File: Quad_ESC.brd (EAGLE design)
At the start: 100 x 80 mm, 25 parts, among them U1 SN74CBTLV3257PWR, Y1 ECS-80-S-4X

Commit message: Lib Update (again)
ok definitely did not push the wrong version of the library file last time haha
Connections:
- net NRST_IN: no longer U$2.P$21
- net SWCLK_IN: no longer U$2.P$19
- net SWDIO_IN: no longer U$2.P$20
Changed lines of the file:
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@@
 <signal name="SWCLK_IN">
 <contactref element="U1" pad="P$4"/>
-<contactref element="U$2" pad="P$19"/>
-<wire x1="-77.47" y1="87.63" x2="-69.85" y2="-10.16" width="0" layer="19" extent="1-1"/>
 </signal>
 <signal name="SWDIO_IN">
 <contactref element="U1" pad="P$7"/>
-<contactref element="U$2" pad="P$20"/>
-<wire x1="-77.47" y1="83.82" x2="-67.31" y2="-10.16" width="0" layer="19" extent="1-1"/>
 </signal>
 <signal name="NRST_IN">
 <contactref element="U1" pad="P$9"/>
-<contactref element="U$2" pad="P$21"/>
-<wire x1="-72.07" y1="82.55" x2="-64.77" y2="-10.16" width="0" layer="19" extent="1-1"/>
 </signal>
 <signal name="N$3">

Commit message: Lib Update/Sch Update
Migrated 3 pin connectors from X-11 AFRO lib; fixed BLHeli symbol so labels no longer overlap; fixed connections and placement on schematic.
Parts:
- added SV2: (no value), con-lsta:FE05-1
- added U$5, U$6, U$7: 3PINCONNECTOR, BLHeli_32 45A:3PINCONNECTOR
- added U$9: BL_HELI45A, BLHeli_32 45A:BLHELI_20X20
- U$1: value BL_HELI45A -> 3PINCONNECTOR; device BLHeli_32 45A:BLHELI_20X20 -> BLHeli_32 45A:3PINCONNECTOR
- moved C10 272.6 mm to (-81.3, -138.4)
- moved U$8 251.8 mm to (-81.3, -134.6)
- moved U$1 15.5 mm to (-72.4, -54.6)
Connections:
- new net ESC1_B: U$1.A, U$9.P$1
- new net ESC1_R: U$1.C, U$9.P$3
- new net ESC1_Y: U$1.B, U$9.P$2
- new net ESC2_B: U$5.A, U$9.P$4
- new net ESC2_R: U$5.C, U$9.P$6
- new net ESC2_Y: U$5.B, U$9.P$5
- new net ESC3_B: U$6.A, U$9.P$7
- new net ESC3_R: U$6.C, U$9.P$9
- new net ESC3_Y: U$6.B, U$9.P$8
- new net ESC4_B: U$7.A, U$9.P$10
- new net ESC4_R: U$7.C, U$9.P$12
- new net ESC4_Y: U$7.B, U$9.P$11
- new net N$31: U$9.P$17
- new net N$32: U$9.P$18
- new net TIM3_CH1: U$4.PA6, U$9.P$19
- new net TIM3_CH2: U$4.PA7, U$9.P$20
- new net TIM3_CH3: U$4.PB0, U$9.P$21
- new net TIM3_CH4: U$4.PB1, U$9.P$22
- net +12V: now also U$9.P$14
- net +3V3: now also SV2.5
- net GND: now also SV2.3, U$9.P$13, U$9.P$15, U$9.P$16
- net NRST_IN: now also SV2.1
- net SWCLK_IN: now also SV2.4
- net SWDIO_IN: now also SV2.2

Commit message: Board Update
Added minor pin connections
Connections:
- removed net N$3: R4.1, U1.P$15
- new net PROG_SEL: R4.1, U$2.P$5, U1.P$15
- net CAN_H: now also U$2.P$6
- net CAN_L: now also U$2.P$7
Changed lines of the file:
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@@
 <wire x1="-72.07" y1="82.55" x2="-78.74" y2="-143.51" width="0" layer="19" extent="1-1"/>
 </signal>
-<signal name="N$3">
+<signal name="PROG_SEL">
 <contactref element="U1" pad="P$15"/>
 <contactref element="R4" pad="1"/>
+<contactref element="U$2" pad="P$5"/>
+<wire x1="-69.85" y1="-12.7" x2="-82.13" y2="-6.35" width="0" layer="19" extent="1-1"/>
 <wire x1="-72.07" y1="90.17" x2="-82.13" y2="-6.35" width="0" layer="19" extent="1-1"/>
 </signal>
@@
 <signal name="CAN_H">
 <contactref element="U$8" pad="CANH"/>
+<contactref element="U$2" pad="P$6"/>
+<wire x1="-67.31" y1="-12.7" x2="-75.88" y2="-132.08" width="0" layer="19" extent="1-1"/>
 </signal>
 <signal name="CAN_L">
 <contactref element="U$8" pad="CANL"/>
+<contactref element="U$2" pad="P$7"/>
+<wire x1="-64.77" y1="-12.7" x2="-75.88" y2="-133.35" width="0" layer="19" extent="1-1"/>
 </signal>
 </signals>

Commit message: Lib/Schem Update
tweaked connections to STM chip; split esc device into lumenier ESC and 8 pin connector (need to figure out how to pair those still :/ ); scooted around components on schematic
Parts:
- removed C12: 0.1uF, SparkFun-Capacitors:0603
- removed R4: 1.5k, SparkFun-Resistors:0603
- removed U1: SN74CBTLV3257PWR, SN74CBTLV3257PWR:SN74CBTLV3257PWR
- BLHELI_ESC: value BL_HELI45A -> BLHeli ESC
- moved R3 336.6 mm to (-81.3, -205.7)
- moved C9 334.8 mm to (-77.5, -201.9)
- moved R1 332.8 mm to (-73.7, -201.9)
- moved C8 317.5 mm to (-81.3, -201.9)
- moved Y1 315.7 mm to (-76.2, -194.3)
- moved R2 300.9 mm to (-81.3, -168.9)
- moved R7 299.0 mm to (-77.5, -168.9)
- moved D1 298.0 mm to (-73.7, -168.9)
- moved C3 281.3 mm to (-81.3, -165.1)
- moved C4 280.9 mm to (-77.5, -165.1)
- moved C7 280.9 mm to (-66.0, -165.1)
- moved C5 280.7 mm to (-73.7, -165.1)
- moved C6 280.7 mm to (-69.8, -165.1)
- moved RESET 278.5 mm to (-78.7, -161.3)
- moved U$4 276.7 mm to (-81.3, -154.9)
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- renumbered U$9 to BLHELI_ESC
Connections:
- removed net N$31: BLHELI_ESC.P$17
- removed net NRST_IN: SV2.1, U1.P$9
- removed net SWCLK1: U1.P$2
- removed net SWCLK_IN: SV2.4, U1.P$4
- removed net SWDIO1: U1.P$5
- removed net SWDIO_IN: SV2.2, U1.P$7
- net +3V3: no longer C12.1, R4.2, U1.P$16
- net ESC1_B: now also BLHELI_ESC.P$17
- net GND: no longer C12.2, U1.P$1, U1.P$8
- net NRST: now also SV2.1; no longer U1.P$11
- net PROG_SEL: no longer R4.1, U1.P$15
- net SWCLK: now also SV2.4
- net SWDIO: now also SV2.2

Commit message: turn off layer 93 (pins). Create correct dimension board
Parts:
- removed BLHELI_ESC: BLHeli ESC, BLHeli_32 45A:BLHELI_20X20
- added U$10: BL_HELI45A, BLHeli_32 45A:BLHELI_20X20
- added U$9: 8PIN_CONNECTOR, BLHeli_32 45A:8PI_CONNECTOR
- moved R3 305.4 mm to (-22.9, 94.0)
- moved R1 301.6 mm to (-15.2, 94.0)
- moved C9 289.6 mm to (-83.8, 87.6)
- moved C8 289.6 mm to (-80.0, 87.6)
- moved C10 274.4 mm to (-87.6, 87.6)
- moved Y1 274.3 mm to (-76.2, 80.0)
- moved R2 270.2 mm to (-19.1, 94.0)
- moved R7 267.8 mm to (-26.7, 94.0)
- moved D1 266.4 mm to (-30.5, 94.0)
- moved SV2 263.4 mm to (-43.2, 87.6)
- moved U$8 259.2 mm to (-88.9, 76.2)
- moved RESET 256.3 mm to (-17.8, 87.6)
- moved C3 253.5 mm to (-61.0, 87.6)
- moved C4 253.0 mm to (-64.8, 87.6)
- moved C7 252.9 mm to (-76.2, 87.6)
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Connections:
- removed net N$32: BLHELI_ESC.P$18
- new net N$6: U$9.P$4
- net +12V: now also U$10.P$14; no longer BLHELI_ESC.P$14
- net ESC1_B: now also U$10.P$1, U$9.P$3; no longer BLHELI_ESC.P$1, BLHELI_ESC.P$17
- net ESC1_R: now also U$10.P$3; no longer BLHELI_ESC.P$3
- net ESC1_Y: now also U$10.P$2; no longer BLHELI_ESC.P$2
- net ESC2_B: now also U$10.P$4; no longer BLHELI_ESC.P$4
- net ESC2_R: now also U$10.P$6; no longer BLHELI_ESC.P$6
- net ESC2_Y: now also U$10.P$5; no longer BLHELI_ESC.P$5
- net ESC3_B: now also U$10.P$7; no longer BLHELI_ESC.P$7
- net ESC3_R: now also U$10.P$9; no longer BLHELI_ESC.P$9
- net ESC3_Y: now also U$10.P$8; no longer BLHELI_ESC.P$8
- net ESC4_B: now also U$10.P$10; no longer BLHELI_ESC.P$10
- net ESC4_R: now also U$10.P$12; no longer BLHELI_ESC.P$12
- net ESC4_Y: now also U$10.P$11; no longer BLHELI_ESC.P$11
- net GND: now also U$10.P$13, U$9.P$1, U$9.P$2; no longer BLHELI_ESC.P$13, BLHELI_ESC.P$15, BLHELI_ESC.P$16
- net TIM3_CH1: now also U$9.P$5; no longer BLHELI_ESC.P$19
- net TIM3_CH2: now also U$9.P$6; no longer BLHELI_ESC.P$20
- net TIM3_CH3: now also U$9.P$7; no longer BLHELI_ESC.P$21
- net TIM3_CH4: now also U$9.P$8; no longer BLHELI_ESC.P$22
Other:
- board size 100 x 80 mm -> 114.3 x 39.9 mm

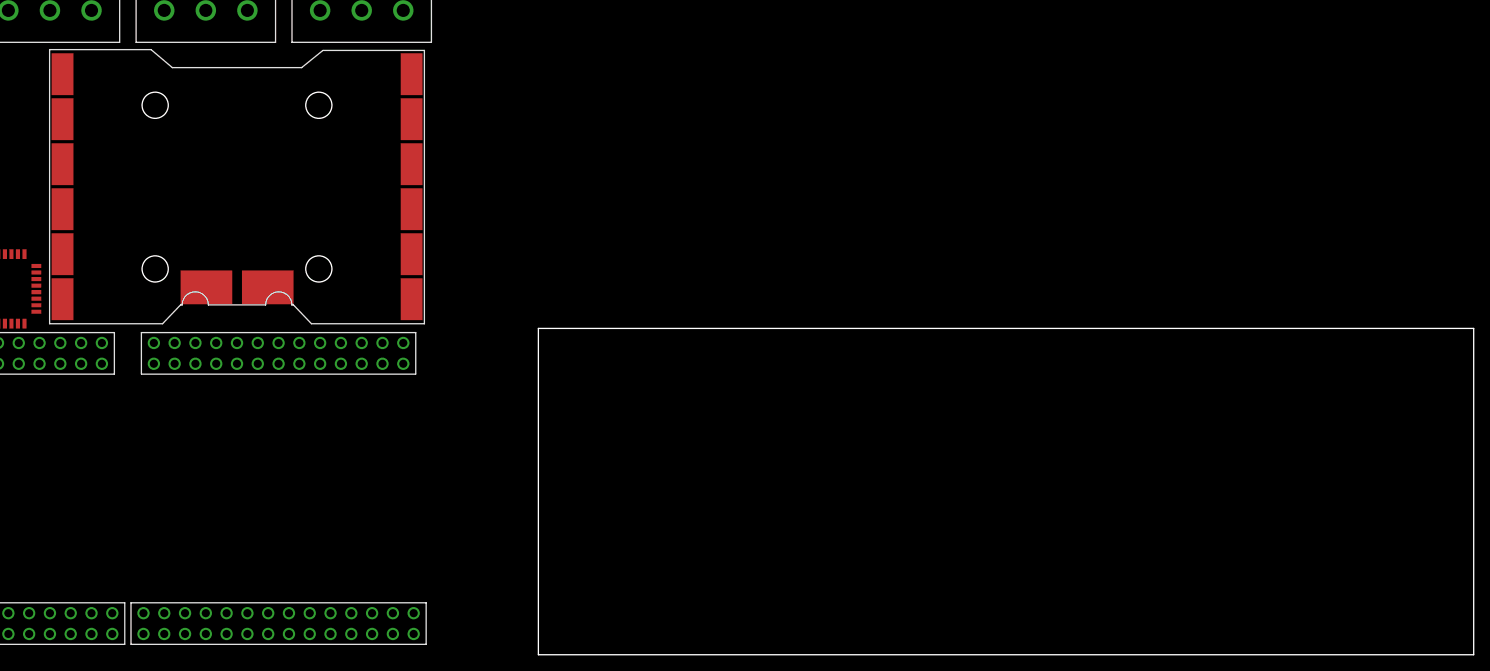
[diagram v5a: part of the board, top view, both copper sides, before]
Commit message: made board a little smaller
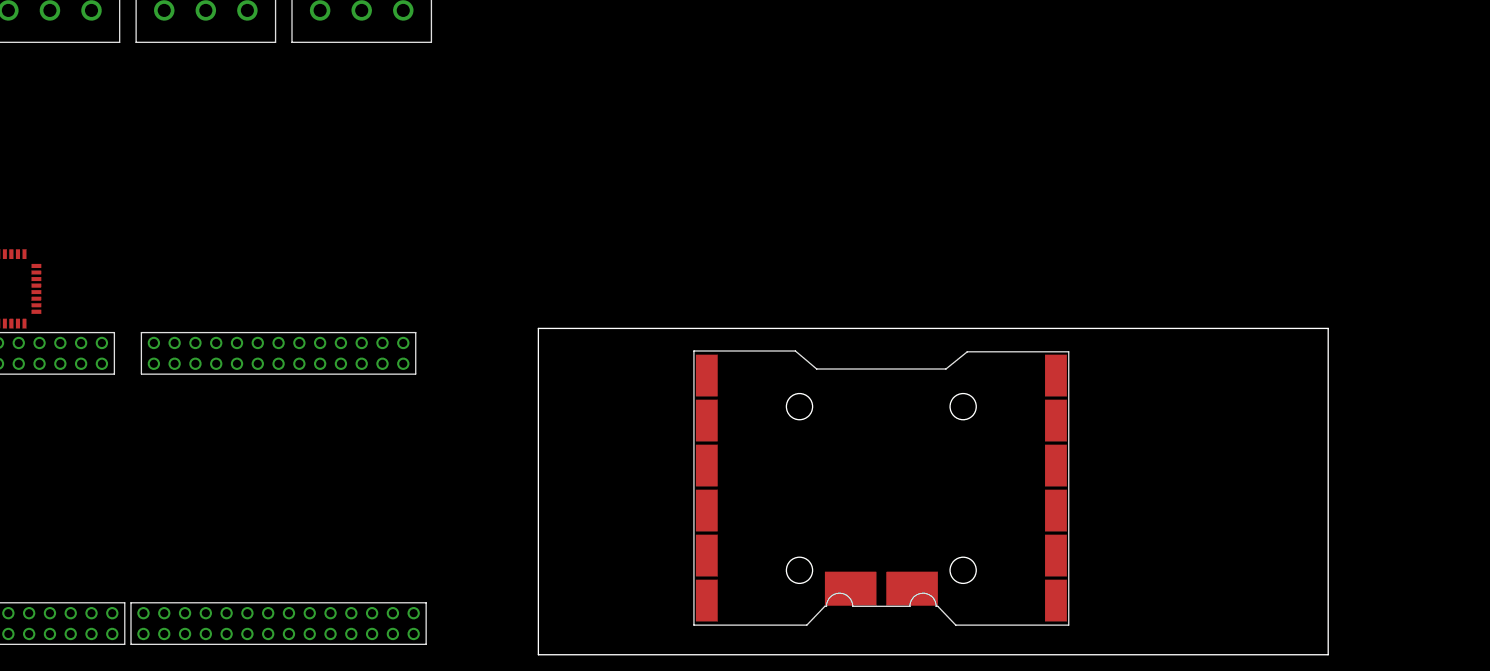
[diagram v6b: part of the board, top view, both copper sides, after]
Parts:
- moved U$10 86.9 mm to (41.9, 20.3)
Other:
- board size 114.3 x 39.9 mm -> 96.5 x 39.9 mm
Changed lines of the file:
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@@
 <board>
 <plain>
-<wire x1="0" y1="0" x2="114.3" y2="0" width="0" layer="20"/>
-<wire x1="114.3" y1="0" x2="114.3" y2="39.878" width="0" layer="20"/>
-<wire x1="114.3" y1="39.878" x2="0" y2="39.878" width="0" layer="20"/>
+<wire x1="0" y1="0" x2="96.52" y2="0" width="0" layer="20"/>
+<wire x1="96.52" y1="0" x2="96.52" y2="39.878" width="0" layer="20"/>
+<wire x1="96.52" y1="39.878" x2="0" y2="39.878" width="0" layer="20"/>
 <wire x1="0" y1="39.878" x2="0" y2="0" width="0" layer="20"/>
 </plain>
@@
 <attribute name="NAME" x="-88.81" y="49.25" size="1.27" layer="21"/>
 </element>
-<element name="U$10" library="BLHeli_32 45A" package="BLHELI_20X20" value="BL_HELI45A" x="-36.83" y="57.15" smashed="yes"/>
+<element name="U$10" library="BLHeli_32 45A" package="BLHELI_20X20" value="BL_HELI45A" x="41.91" y="20.32" smashed="yes"/>
 <element name="U$2" library="ESC_to_Backplane_Connectors" package="ESC2BACKPLANE_WHOLE" value="ESC2BACKPLANE" x="-48.26" y="3.81" smashed="yes"/>
 <element name="U$3" library="ESC_to_Backplane_Connectors" package="ESC2BACKPLANE_WHOLE" value="ESC2BACKPLANE" x="-85.09" y="3.81" smashed="yes"/>
@@
 <wire x1="-41.91" y1="38.1" x2="-41.91" y2="35.56" width="0" layer="19" extent="1-1"/>
 <wire x1="-39.37" y1="38.1" x2="-39.37" y2="35.56" width="0" layer="19" extent="1-1"/>
-<wire x1="-40.571" y1="44.903" x2="-39.37" y2="38.1" width="0" layer="19" extent="1-1"/>
+<wire x1="38.169" y1="8.073" x2="-39.37" y2="38.1" width="0" layer="19" extent="1-1"/>
 <wire x1="-52.07" y1="5.08" x2="-46.99" y2="35.56" width="0" layer="19" extent="1-1"/>
 <wire x1="-52.07" y1="2.54" x2="-52.07" y2="5.08" width="0" layer="19" extent="1-1"/>
@@
 <wire x1="-24.13" y1="38.1" x2="-24.13" y2="35.56" width="0" layer="19" extent="1-1"/>
 <wire x1="-26.67" y1="38.1" x2="-26.67" y2="35.56" width="0" layer="19" extent="1-1"/>
-<wire x1="-33.071" y1="44.903" x2="-26.67" y2="38.1" width="0" layer="19" extent="1-1"/>
+<wire x1="45.669" y1="8.073" x2="-26.67" y2="38.1" width="0" layer="19" extent="1-1"/>
 </signal>
 <signal name="PROG_SEL">
@@
 <contactref element="U$7" pad="A"/>
 <contactref element="U$10" pad="P$10"/>
-<wire x1="-64.77" y1="78.74" x2="-15.49" y2="54.449" width="0" layer="19" extent="1-1"/>
+<wire x1="-64.77" y1="78.74" x2="63.25" y2="17.619" width="0" layer="19" extent="1-1"/>
 </signal>
 <signal name="ESC4_Y">
 <contactref element="U$7" pad="B"/>
 <contactref element="U$10" pad="P$11"/>
-<wire x1="-59.69" y1="78.74" x2="-15.49" y2="48.949" width="0" layer="19" extent="1-1"/>
+<wire x1="-59.69" y1="78.74" x2="63.25" y2="12.119" width="0" layer="19" extent="1-1"/>
 </signal>
 <signal name="ESC4_R">
 <contactref element="U$7" pad="C"/>
 <contactref element="U$10" pad="P$12"/>
-<wire x1="-54.61" y1="78.74" x2="-15.49" y2="43.449" width="0" layer="19" extent="1-1"/>
+<wire x1="-54.61" y1="78.74" x2="63.25" y2="6.619" width="0" layer="19" extent="1-1"/>
 </signal>
 <signal name="ESC3_B">
 <contactref element="U$6" pad="A"/>
 <contactref element="U$10" pad="P$7"/>
-<wire x1="-45.72" y1="78.74" x2="-15.49" y2="70.949" width="0" layer="19" extent="1-1"/>
+<wire x1="-45.72" y1="78.74" x2="63.25" y2="34.119" width="0" layer="19" extent="1-1"/>
 </signal>
 <signal name="ESC3_Y">
 <contactref element="U$6" pad="B"/>
 <contactref element="U$10" pad="P$8"/>
-<wire x1="-40.64" y1="78.74" x2="-15.49" y2="65.449" width="0" layer="19" extent="1-1"/>
+<wire x1="-40.64" y1="78.74" x2="63.25" y2="28.619" width="0" layer="19" extent="1-1"/>
 </signal>
 <signal name="ESC3_R">
 <contactref element="U$6" pad="C"/>
 <contactref element="U$10" pad="P$9"/>
-<wire x1="-15.49" y1="59.949" x2="-35.56" y2="78.74" width="0" layer="19" extent="1-1"/>
+<wire x1="63.25" y1="23.119" x2="-35.56" y2="78.74" width="0" layer="19" extent="1-1"/>
 </signal>
 <signal name="ESC2_B">
 <contactref element="U$5" pad="A"/>
 <contactref element="U$10" pad="P$4"/>
-<wire x1="-58.152" y1="54.449" x2="-26.67" y2="78.74" width="0" layer="19" extent="1-1"/>
+<wire x1="20.588" y1="17.619" x2="-26.67" y2="78.74" width="0" layer="19" extent="1-1"/>
 </signal>
 <signal name="ESC2_Y">
 <contactref element="U$5" pad="B"/>
 <contactref element="U$10" pad="P$5"/>
-<wire x1="-58.152" y1="48.949" x2="-21.59" y2="78.74" width="0" layer="19" extent="1-1"/>
+<wire x1="20.588" y1="12.119" x2="-21.59" y2="78.74" width="0" layer="19" extent="1-1"/>
 </signal>
 <signal name="ESC2_R">
 <contactref element="U$5" pad="C"/>
 <contactref element="U$10" pad="P$6"/>
-<wire x1="-58.152" y1="43.449" x2="-16.51" y2="78.74" width="0" layer="19" extent="1-1"/>
+<wire x1="20.588" y1="6.619" x2="-16.51" y2="78.74" width="0" layer="19" extent="1-1"/>
 </signal>
 <signal name="ESC1_B">
@@
 <contactref element="U$10" pad="P$1"/>
 <contactref element="U$9" pad="P$3"/>
-<wire x1="-58.152" y1="70.949" x2="-29.52" y2="87.38" width="0" layer="19" extent="1-1"/>
-<wire x1="-85.09" y1="44.45" x2="-58.152" y2="70.949" width="0" layer="19" extent="1-1"/>
+<wire x1="20.588" y1="34.119" x2="-29.52" y2="87.38" width="0" layer="19" extent="1-1"/>
+<wire x1="-85.09" y1="44.45" x2="20.588" y2="34.119" width="0" layer="19" extent="1-1"/>
 </signal>
 <signal name="ESC1_Y">
 <contactref element="U$1" pad="B"/>
 <contactref element="U$10" pad="P$2"/>
-<wire x1="-58.152" y1="65.449" x2="-80.01" y2="44.45" width="0" layer="19" extent="1-1"/>
+<wire x1="20.588" y1="28.619" x2="-80.01" y2="44.45" width="0" layer="19" extent="1-1"/>
 </signal>
 <signal name="ESC1_R">
 <contactref element="U$1" pad="C"/>
 <contactref element="U$10" pad="P$3"/>
-<wire x1="-58.152" y1="59.949" x2="-74.93" y2="44.45" width="0" layer="19" extent="1-1"/>
+<wire x1="20.588" y1="23.119" x2="-74.93" y2="44.45" width="0" layer="19" extent="1-1"/>
 </signal>
 <signal name="CAN_H">
